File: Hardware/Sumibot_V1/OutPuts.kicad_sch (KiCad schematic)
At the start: 8 parts, among them Q5 DMG3406L

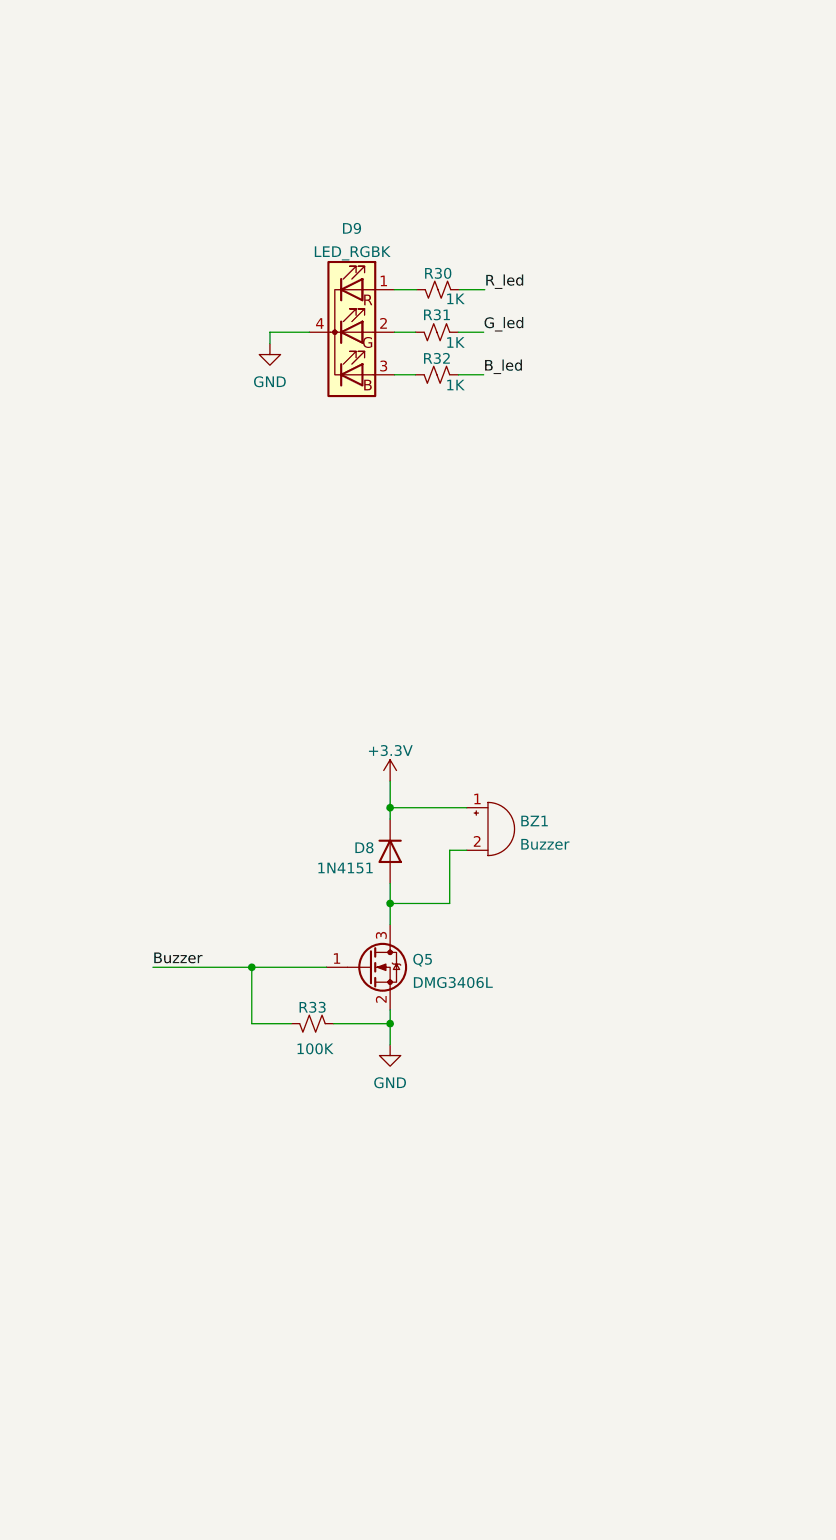
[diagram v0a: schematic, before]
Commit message: Añadi DAC_Speaker y renombre carpeta kicad
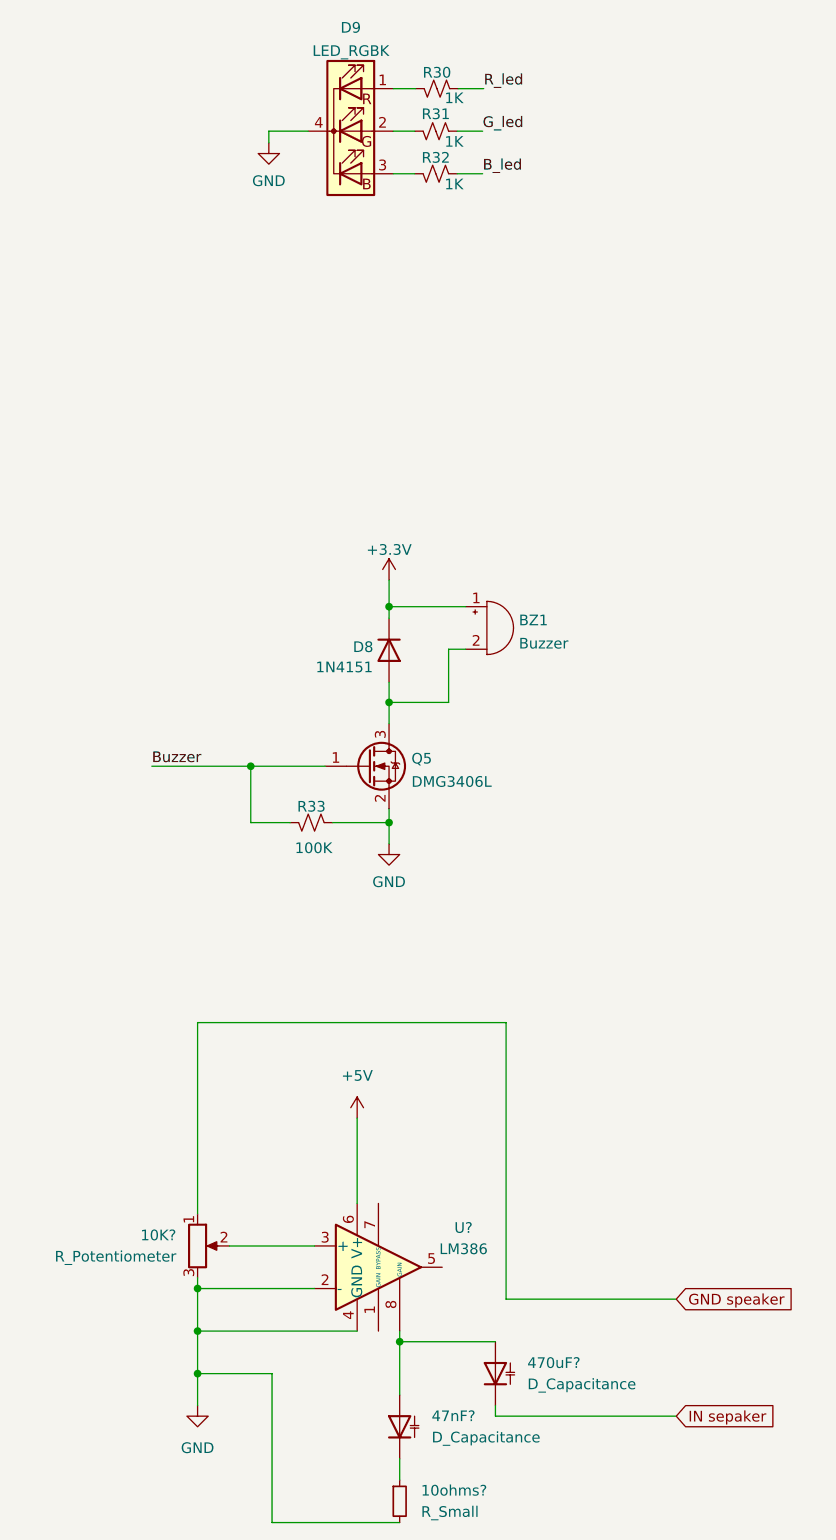
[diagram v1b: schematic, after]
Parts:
- added 10K?: R_Potentiometer, symbol Device:R_Potentiometer
- added 10ohms?: R_Small, symbol Device:R_Small
- added 470uF?, 47nF?: D_Capacitance, symbol Device:D_Capacitance
- added U?: LM386, symbol Amplifier_Audio:LM386
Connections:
- net GND: now also 10K?.3, 10ohms?.2, U?.2 (-), U?.4 (GND)
- new net: 10K?.2, U?.3 (+)
- new net: 470uF?.2 (A), 47nF?.2 (A), U?.8 (GAIN)
- new net: 10ohms?.1, 47nF?.1 (K)
- new net +5V: U?.6 (V+)
- new net GND speaker: 10K?.1
- new net IN sepaker: 470uF?.1 (K)
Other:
- moved on the sheet: BZ1, D8, D9, Q5, R30, R31, R32, R33
